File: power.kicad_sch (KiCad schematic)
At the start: 26 parts, among them J3 Battery, U2 BQ24072RGTT, U3 TPS63020DSJR

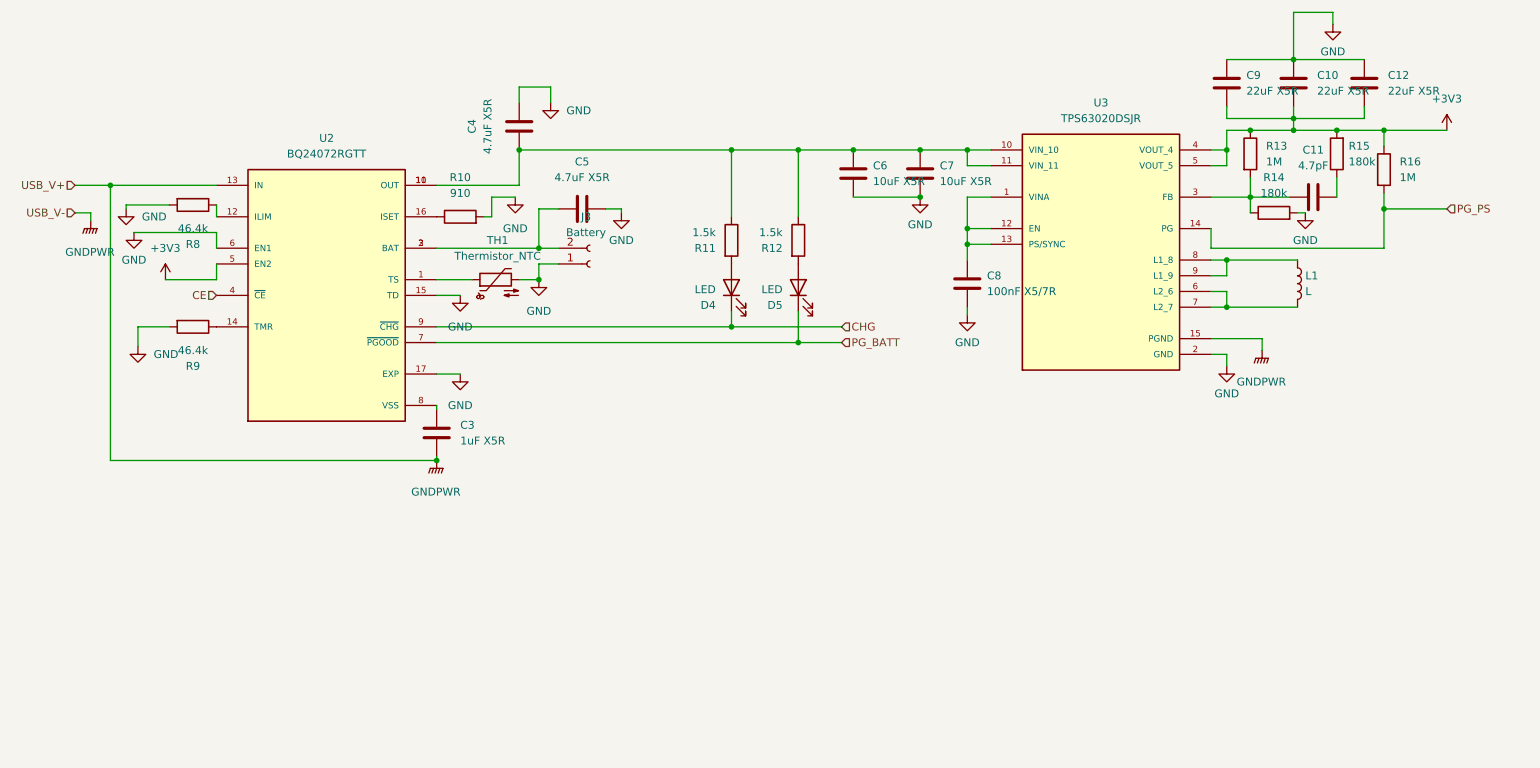
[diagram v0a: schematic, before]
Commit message: USB IC Removal
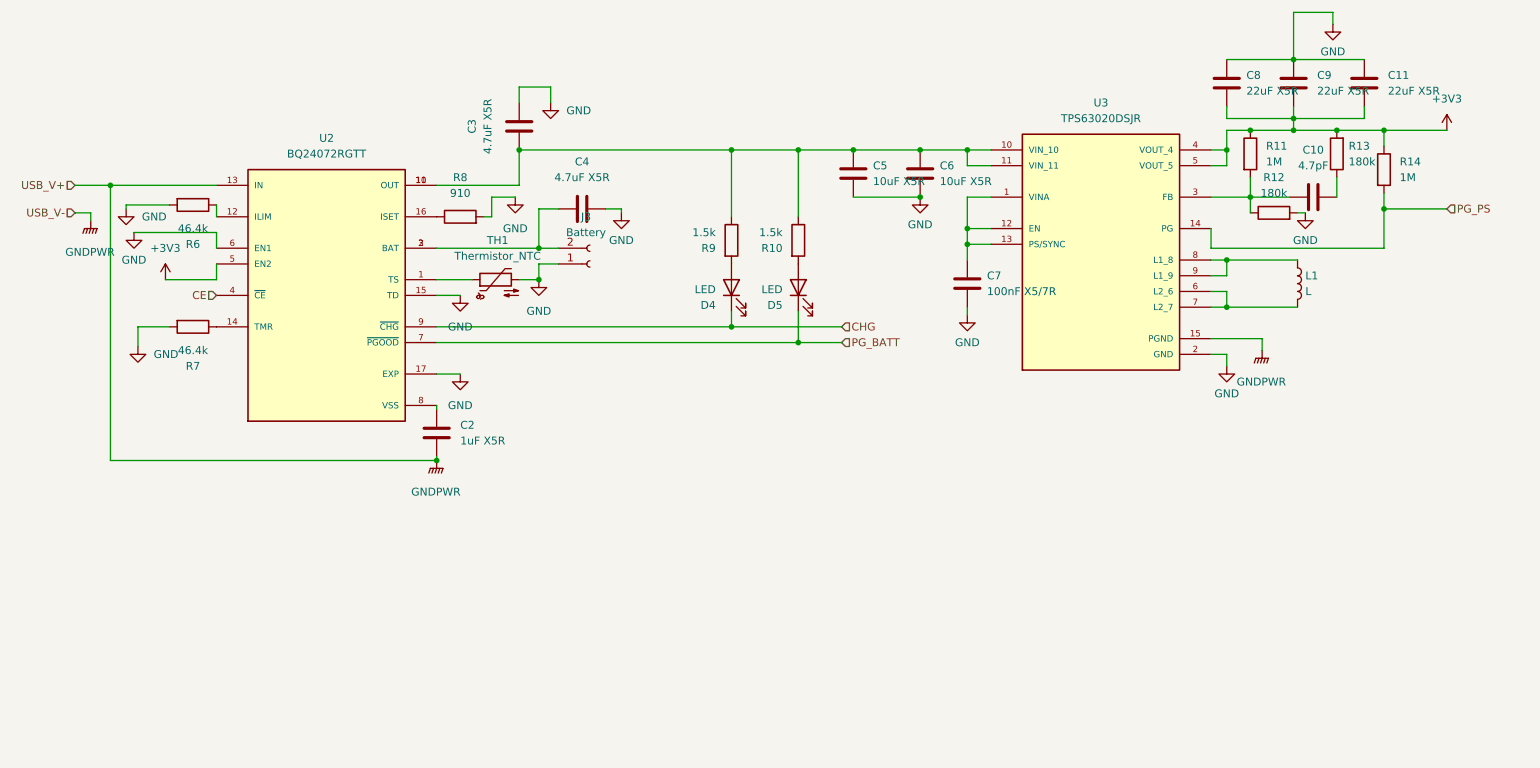
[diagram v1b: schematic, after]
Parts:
- renumbered C11 to C10, C12 to C11, C3 to C2, C4 to C3, C5 to C4, C6 to C5, C7 to C6, C8 to C7, C9 to C8, C10 to C9, R12 to R10, R13 to R11, R14 to R12, R15 to R13, R16 to R14, R8 to R6, R9 to R7, R10 to R8, R11 to R9

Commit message: One piece board, a bit into PCB
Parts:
- C2: footprint Capacitor_SMD:C_0402_1005Metric -> Capacitor_SMD:C_1206_3216Metric
- C3, C4: footprint Capacitor_SMD:C_0402_1005Metric -> Capacitor_SMD:C_0805_2012Metric
- C5, C6: footprint Capacitor_SMD:C_0402_1005Metric -> Capacitor_SMD:C_0603_1608Metric
- L1: value L -> 1.5uH
- R8: footprint Resistor_SMD:R_0402_1005Metric -> Resistor_SMD:R_0603_1608Metric
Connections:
- net GND: no longer C11.1, C3.2, C4.2, C5.2, C6.2, C8.1, C9.1, J3.1 (Pin_1), TH1.2
- net GNDPWR: now also C11.1, C3.2, C4.2, C5.2, C6.2, C8.1, C9.1, J3.1 (Pin_1), TH1.2, U2.8 (VSS); no longer U2.13 (IN)
- net USB_V+: now reaches C2.1
- net USB_V+: now also U2.13 (IN); no longer U2.8 (VSS)
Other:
- moved on the sheet: C2

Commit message: All Routed!
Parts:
- L1: footprint JLCPCB:MPIT4030 -> lib_fp:MPIT4030; MPN (none) -> C281291
- U3: renamed from U2; footprint JLCPCB:IC_BQ24072RGTT -> lib_fp:IC_BQ24072RGTT; MANUFACTURER Texas Instruments -> (none); MAXIMUM_PACKAGE_HEIGHT 1 mm -> (none); MPN (none) -> C140288; PARTREV N -> (none); STANDARD Manufacturer Recommendations -> (none)
- U4: renamed from U3; footprint JLCPCB:IC_TPS63020DSJR -> lib_fp:IC_TPS63020DSJR; Availability Good -> (none); DigiKey-Purchase-URL https://snapeda.com/shop?store=DigiKey&id=296571 -> (none); MF Texas Instruments -> (none); MP TPS63020DSJR -> (none); MPN (none) -> C15483; Mouser-Purchase-URL https://snapeda.com/shop?store=Mouser&id=296571 -> (none); Package VSON-14 Texas Instruments -> (none); Price None -> (none); Texas_Instruments-Purchase-URL https://snapeda.com/shop?store=Texas+Instruments&id=296571 -> (none)
- renumbered C4 to C10, C5 to C11, C6 to C12, C7 to C13, C8 to C14, C9 to C15, C10 to C16, C11 to C17, C2 to C8, C3 to C9, J3 to J5, R8 to R10, R9 to R11, R10 to R12, R11 to R13, R12 to R14, R13 to R15, R14 to R16, R6 to R8, R7 to R9
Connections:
- net +3V3: now also R11.1, R12.1
- net GND: no longer U3.17 (EXP), U3.6 (EN1)
- net GNDPWR: now also U3.17 (EXP), U3.6 (EN1)
- net at C11.1, C12.1, C9.1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: no longer R11.1, R12.1

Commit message: Before Shortening
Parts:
- D4: value LED -> GREEN LED; footprint LED_SMD:LED_0402_1005Metric -> LED_SMD:LED_0603_1608Metric; MPN (none) -> C72043
- D5: value LED -> YELLOW LED; footprint LED_SMD:LED_0402_1005Metric -> LED_SMD:LED_0603_1608Metric; MPN (none) -> C72038
- J5: footprint Connector_JST:JST_SH_SM02B-SRSS-TB_1x02-1MP_P1.00mm_Horizontal -> JLCPCB:XH-2PWB; MPN (none) -> C64520
- R11: value 1.5k -> 1
- R12: value 1.5k -> 68
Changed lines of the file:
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@@
       (effects (font (size 1.27 1.27)) (justify left))
     )
-    (property "Value" "LED" (id 1) (at 139.065 66.3576 90)
-      (effects (font (size 1.27 1.27)) (justify left))
-    )
-    (property "Footprint" "LED_SMD:LED_0402_1005Metric" (id 2) (at 141.605 66.04 0)
+    (property "Value" "GREEN LED" (id 1) (at 139.065 66.3576 90)
+      (effects (font (size 1.27 1.27)) (justify left))
+    )
+    (property "Footprint" "LED_SMD:LED_0603_1608Metric" (id 2) (at 141.605 66.04 0)
       (effects (font (size 1.27 1.27)) hide)
     )
     (property "Datasheet" "~" (id 3) (at 141.605 66.04 0)
+      (effects (font (size 1.27 1.27)) hide)
+    )
+    (property "MPN" "C72043" (id 4) (at 141.605 66.04 90)
       (effects (font (size 1.27 1.27)) hide)
     )
@@
       (effects (font (size 1.27 1.27)) (justify right))
     )
-    (property "Value" "1.5k" (id 1) (at 149.86 57.1501 0)
+    (property "Value" "68" (id 1) (at 149.86 57.1501 0)
       (effects (font (size 1.27 1.27)) (justify right))
     )
@@
     (property "Reference" "J5" (id 0) (at 118.11 54.61 0))
     (property "Value" "Battery" (id 1) (at 118.11 57.15 0))
-    (property "Footprint" "Connector_JST:JST_SH_SM02B-SRSS-TB_1x02-1MP_P1.00mm_Horizontal" (id 2) (at 118.745 62.23 0)
+    (property "Footprint" "JLCPCB:XH-2PWB" (id 2) (at 118.745 62.23 0)
       (effects (font (size 1.27 1.27)) hide)
     )
     (property "Datasheet" "~" (id 3) (at 118.745 62.23 0)
+      (effects (font (size 1.27 1.27)) hide)
+    )
+    (property "MPN" "C64520" (id 4) (at 118.745 62.23 0)
       (effects (font (size 1.27 1.27)) hide)
     )
@@
       (effects (font (size 1.27 1.27)) (justify left))
     )
-    (property "Value" "LED" (id 1) (at 149.86 66.3576 90)
-      (effects (font (size 1.27 1.27)) (justify left))
-    )
-    (property "Footprint" "LED_SMD:LED_0402_1005Metric" (id 2) (at 152.4 66.04 0)
+    (property "Value" "YELLOW LED" (id 1) (at 149.86 66.3576 90)
+      (effects (font (size 1.27 1.27)) (justify left))
+    )
+    (property "Footprint" "LED_SMD:LED_0603_1608Metric" (id 2) (at 152.4 66.04 0)
       (effects (font (size 1.27 1.27)) hide)
     )
     (property "Datasheet" "~" (id 3) (at 152.4 66.04 0)
+      (effects (font (size 1.27 1.27)) hide)
+    )
+    (property "MPN" "C72038" (id 4) (at 152.4 66.04 90)
       (effects (font (size 1.27 1.27)) hide)
     )
@@
       (effects (font (size 1.27 1.27)) (justify right))
     )
-    (property "Value" "1.5k" (id 1) (at 139.065 57.1501 0)
+    (property "Value" "1" (id 1) (at 139.065 57.1501 0)
       (effects (font (size 1.27 1.27)) (justify right))
     )

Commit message: New Audio
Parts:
- J5: footprint JLCPCB:XH-2PWB -> Connector_JST:JST_SH_SM02B-SRSS-TB_1x02-1MP_P1.00mm_Horizontal
- renumbered D4 to D2, D5 to D3, R12 to R10, R13 to R11, R14 to R12, R15 to R13, R16 to R14, R8 to R6, R9 to R7, R10 to R8, R11 to R9
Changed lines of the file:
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@@
   (symbol (lib_id "power:GNDPWR") (at 97.79 80.01 0) (unit 1)
     (in_bom yes) (on_board yes) (fields_autoplaced)
-    (property "Reference" "#PWR0106" (id 0) (at 97.79 85.09 0)
+    (property "Reference" "#PWR029" (id 0) (at 97.79 85.09 0)
       (effects (font (size 1.27 1.27)) hide)
     )
@@
   (symbol (lib_id "Device:R") (at 239.395 44.45 180) (unit 1)
     (in_bom yes) (on_board yes) (fields_autoplaced)
-    (property "Reference" "R15" (id 0) (at 241.3 43.1799 0)
+    (property "Reference" "R13" (id 0) (at 241.3 43.1799 0)
       (effects (font (size 1.27 1.27)) (justify right))
     )
@@
   (symbol (lib_id "power:GNDPWR") (at 238.76 23.495 0) (unit 1)
     (in_bom yes) (on_board yes) (fields_autoplaced)
-    (property "Reference" "#PWR039" (id 0) (at 238.76 28.575 0)
+    (property "Reference" "#PWR040" (id 0) (at 238.76 28.575 0)
       (effects (font (size 1.27 1.27)) hide)
     )
@@
   (symbol (lib_id "Device:R") (at 225.425 44.45 0) (unit 1)
     (in_bom yes) (on_board yes) (fields_autoplaced)
-    (property "Reference" "R13" (id 0) (at 227.965 43.1799 0)
+    (property "Reference" "R11" (id 0) (at 227.965 43.1799 0)
       (effects (font (size 1.27 1.27)) (justify left))
     )
@@
   (symbol (lib_id "power:GND") (at 179.705 70.485 0) (unit 1)
     (in_bom yes) (on_board yes) (fields_autoplaced)
-    (property "Reference" "#PWR035" (id 0) (at 179.705 76.835 0)
+    (property "Reference" "#PWR036" (id 0) (at 179.705 76.835 0)
       (effects (font (size 1.27 1.27)) hide)
     )
@@
   (symbol (lib_id "power:GNDPWR") (at 227.33 76.2 0) (unit 1)
     (in_bom yes) (on_board yes) (fields_autoplaced)
-    (property "Reference" "#PWR037" (id 0) (at 227.33 81.28 0)
+    (property "Reference" "#PWR038" (id 0) (at 227.33 81.28 0)
       (effects (font (size 1.27 1.27)) hide)
     )
@@
   (symbol (lib_id "Device:R") (at 54.61 52.705 270) (unit 1)
     (in_bom yes) (on_board yes) (fields_autoplaced)
-    (property "Reference" "R8" (id 0) (at 54.61 59.055 90))
+    (property "Reference" "R6" (id 0) (at 54.61 59.055 90))
     (property "Value" "46.4k" (id 1) (at 54.61 56.515 90))
     (property "Footprint" "Resistor_SMD:R_0402_1005Metric" (id 2) (at 54.61 50.927 90)
@@
   (symbol (lib_id "Device:R") (at 229.235 53.975 90) (unit 1)
     (in_bom yes) (on_board yes) (fields_autoplaced)
-    (property "Reference" "R14" (id 0) (at 229.235 48.26 90))
+    (property "Reference" "R12" (id 0) (at 229.235 48.26 90))
     (property "Value" "180k" (id 1) (at 229.235 50.8 90))
     (property "Footprint" "Resistor_SMD:R_0402_1005Metric" (id 2) (at 229.235 55.753 90)
@@
   (symbol (lib_id "power:GNDPWR") (at 45.085 57.15 0) (unit 1)
     (in_bom yes) (on_board yes) (fields_autoplaced)
-    (property "Reference" "#PWR0105" (id 0) (at 45.085 62.23 0)
+    (property "Reference" "#PWR024" (id 0) (at 45.085 62.23 0)
       (effects (font (size 1.27 1.27)) hide)
     )
@@
   (symbol (lib_id "power:GNDPWR") (at 172.085 51.435 0) (unit 1)
     (in_bom yes) (on_board yes) (fields_autoplaced)
-    (property "Reference" "#PWR034" (id 0) (at 172.085 56.515 0)
+    (property "Reference" "#PWR035" (id 0) (at 172.085 56.515 0)
       (effects (font (size 1.27 1.27)) hide)
     )
@@
   (symbol (lib_id "Device:LED") (at 141.605 66.04 90) (unit 1)
     (in_bom yes) (on_board yes) (fields_autoplaced)
-    (property "Reference" "D4" (id 0) (at 139.065 68.8976 90)
+    (property "Reference" "D2" (id 0) (at 139.065 68.8976 90)
       (effects (font (size 1.27 1.27)) (justify left))
     )
@@
   (symbol (lib_id "Device:R") (at 152.4 58.42 0) (unit 1)
     (in_bom yes) (on_board yes) (fields_autoplaced)
-    (property "Reference" "R12" (id 0) (at 149.86 59.6901 0)
+    (property "Reference" "R10" (id 0) (at 149.86 59.6901 0)
       (effects (font (size 1.27 1.27)) (justify right))
     )
@@
     (property "Reference" "J5" (id 0) (at 118.11 54.61 0))
     (property "Value" "Battery" (id 1) (at 118.11 57.15 0))
-    (property "Footprint" "JLCPCB:XH-2PWB" (id 2) (at 118.745 62.23 0)
+    (property "Footprint" "Connector_JST:JST_SH_SM02B-SRSS-TB_1x02-1MP_P1.00mm_Horizontal" (id 2) (at 118.745 62.23 0)
       (effects (font (size 1.27 1.27)) hide)
     )
@@
   (symbol (lib_id "Device:LED") (at 152.4 66.04 90) (unit 1)
     (in_bom yes) (on_board yes) (fields_autoplaced)
-    (property "Reference" "D5" (id 0) (at 149.86 68.8976 90)
+    (property "Reference" "D3" (id 0) (at 149.86 68.8976 90)
       (effects (font (size 1.27 1.27)) (justify left))
     )
@@
   (symbol (lib_id "power:+3V3") (at 147.32 54.61 0) (unit 1)
     (in_bom yes) (on_board yes) (fields_autoplaced)
-    (property "Reference" "#PWR0107" (id 0) (at 147.32 58.42 0)
+    (property "Reference" "#PWR034" (id 0) (at 147.32 58.42 0)
       (effects (font (size 1.27 1.27)) hide)
     )
@@
   (symbol (lib_id "power:GND") (at 234.315 53.975 0) (unit 1)
     (in_bom yes) (on_board yes) (fields_autoplaced)
-    (property "Reference" "#PWR038" (id 0) (at 234.315 60.325 0)
+    (property "Reference" "#PWR039" (id 0) (at 234.315 60.325 0)
       (effects (font (size 1.27 1.27)) hide)
     )
@@
   (symbol (lib_id "power:+3V3") (at 257.175 40.64 0) (unit 1)
     (in_bom yes) (on_board yes) (fields_autoplaced)
-    (property "Reference" "#PWR040" (id 0) (at 257.175 44.45 0)
+    (property "Reference" "#PWR041" (id 0) (at 257.175 44.45 0)
       (effects (font (size 1.27 1.27)) hide)
     )
@@
   (symbol (lib_id "Device:R") (at 54.61 72.39 270) (unit 1)
     (in_bom yes) (on_board yes) (fields_autoplaced)
-    (property "Reference" "R9" (id 0) (at 54.61 78.74 90))
+    (property "Reference" "R7" (id 0) (at 54.61 78.74 90))
     (property "Value" "46.4k" (id 1) (at 54.61 76.2 90))
     (property "Footprint" "Resistor_SMD:R_0402_1005Metric" (id 2) (at 54.61 70.612 90)
@@
   (symbol (lib_id "power:GND") (at 221.615 78.74 0) (unit 1)
     (in_bom yes) (on_board yes) (fields_autoplaced)
-    (property "Reference" "#PWR036" (id 0) (at 221.615 85.09 0)
+    (property "Reference" "#PWR037" (id 0) (at 221.615 85.09 0)
       (effects (font (size 1.27 1.27)) hide)
     )
@@
   (symbol (lib_id "Device:R") (at 247.015 46.99 0) (unit 1)
     (in_bom yes) (on_board yes) (fields_autoplaced)
-    (property "Reference" "R16" (id 0) (at 249.555 45.7199 0)
+    (property "Reference" "R14" (id 0) (at 249.555 45.7199 0)
       (effects (font (size 1.27 1.27)) (justify left))
     )
@@
   (symbol (lib_id "Device:R") (at 97.79 54.61 90) (unit 1)
     (in_bom yes) (on_board yes) (fields_autoplaced)
-    (property "Reference" "R10" (id 0) (at 97.79 48.26 90))
+    (property "Reference" "R8" (id 0) (at 97.79 48.26 90))
     (property "Value" "910" (id 1) (at 97.79 50.8 90))
     (property "Footprint" "Resistor_SMD:R_0603_1608Metric" (id 2) (at 97.79 56.388 90)
@@
   (symbol (lib_id "Device:R") (at 141.605 58.42 0) (unit 1)
     (in_bom yes) (on_board yes) (fields_autoplaced)
-    (property "Reference" "R11" (id 0) (at 139.065 59.6901 0)
+    (property "Reference" "R9" (id 0) (at 139.065 59.6901 0)
       (effects (font (size 1.27 1.27)) (justify right))
     )

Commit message: Getting There
Need to move keyboard down and finish routing to audio, then we're there!
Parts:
- C3: renamed from C8; value 1uF X5R -> 1uF X7R; MPN (none) -> C1848
- R12, R13: footprint Resistor_SMD:R_0402_1005Metric -> Resistor_SMD:R_0603_1608Metric
- renumbered C15 to C10, C16 to C11, C17 to C12, C9 to C4, C10 to C5, C11 to C6, C12 to C7, C13 to C8, C14 to C9, U3 to U2, U4 to U3

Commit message: First JLCPCB Ship!
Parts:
- removed C12, C9: 22uF X5R, Capacitor_SMD:C_0402_1005Metric, symbol Device:C
- added C? (x2): 22uF X5R, Capacitor_SMD:C_0603_1608Metric, symbol Device:C
- C12: renamed from C4; MPN (none) -> C1779
- C13: renamed from C5; MPN (none) -> C1779
- C14: renamed from C6; MPN (none) -> C96446
- C15: renamed from C7; MPN (none) -> C96446
- C16: renamed from C8; MPN (none) -> C1525
- C18: renamed from C10; footprint Capacitor_SMD:C_0402_1005Metric -> Capacitor_SMD:C_0603_1608Metric; MPN (none) -> C59461
- C19: renamed from C11; MPN (none) -> C1569
- J5: MPN C64520 -> C160402
- R10: M[N (none) -> C25133
- R11, R14: MPN (none) -> C26083
- R12, R13: MPN (none) -> C22827
- R6, R7: MPN (none) -> C25792
- R8: MPN (none) -> C21190
- R9: MPN (none) -> C25086
- TH1: now left out of the parts list
- renumbered C3 to C11
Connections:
- net +3V3: now also C?.2, C?.2
- net GNDPWR: now also C?.1, C?.1
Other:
- moved on the sheet: C11, C12, C13, C14, C15, C16, C18, C19, D2, D3, J5, L1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
